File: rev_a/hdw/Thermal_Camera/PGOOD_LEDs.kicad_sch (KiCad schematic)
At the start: 21 parts, among them U1501 74LVC1G97, U1502 74LVC1G97, U1503 74LVC1G97, U1504 74LVC1G97, U1505 74LVC1G97

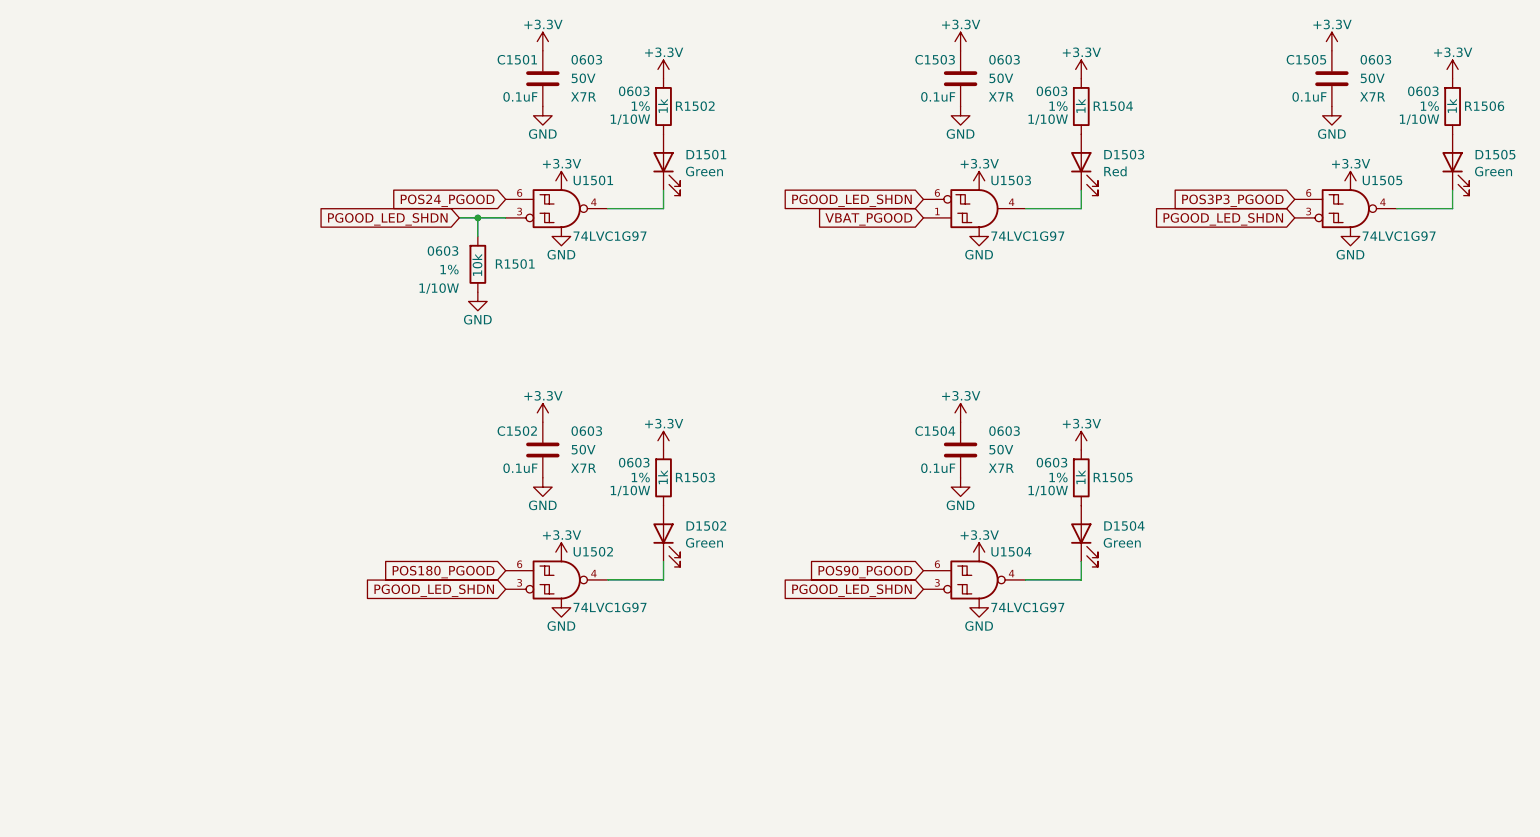
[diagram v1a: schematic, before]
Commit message: added many more blank schematic sheets
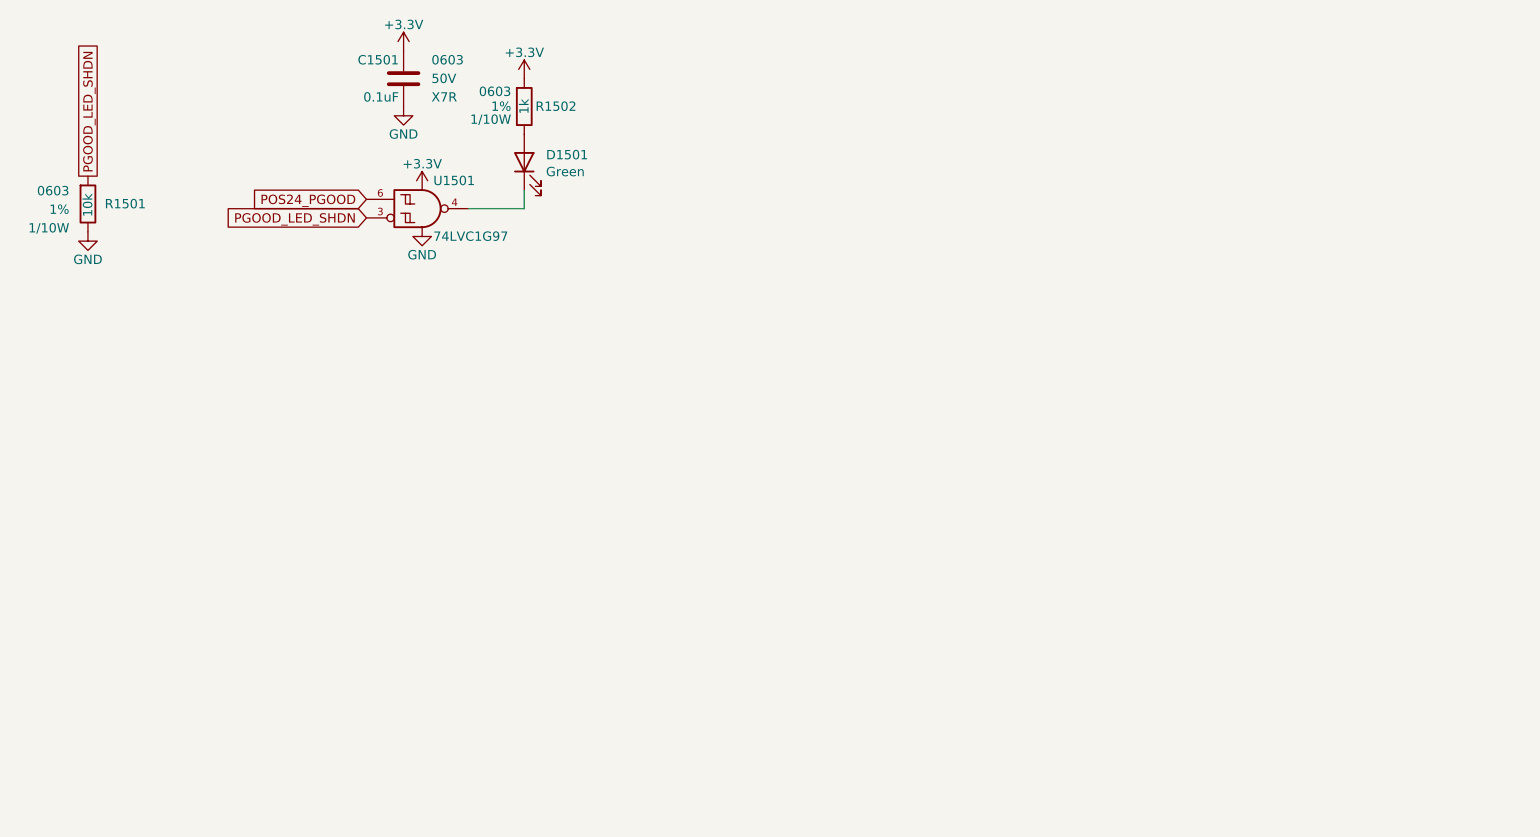
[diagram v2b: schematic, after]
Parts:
- removed C1502, C1503, C1504, C1505: 0.1uF, Capacitors_SMD:C_0603, symbol Custom_Library:C_Custom
- removed D1502, D1504, D1505: Green, LEDs:LED_0603, symbol Device:LED
- removed D1503: Red, LEDs:LED_0603, symbol Device:LED
- removed R1503, R1504, R1505, R1506: 1k, Resistors_SMD:R_0603, symbol Custom_Library:R_Custom
- removed U1502, U1504, U1505: 74LVC1G97, Package_TO_SOT_SMD:SOT-363_SC-70-6, symbol Custom_Library:74LVC1G97_Power_NAND_INV
- removed U1503: 74LVC1G97, Package_TO_SOT_SMD:SOT-363_SC-70-6, symbol Custom_Library:74LVC1G97_Power_AND_INV
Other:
- moved on the sheet: C1501, D1501, R1501, R1502, U1501

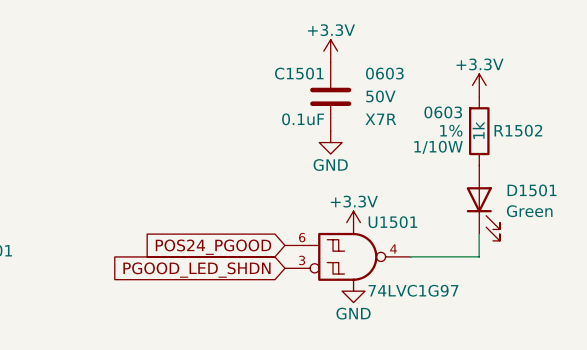
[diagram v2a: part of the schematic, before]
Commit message: changed a lot of circuits from +3.3V to +3.0V VDD
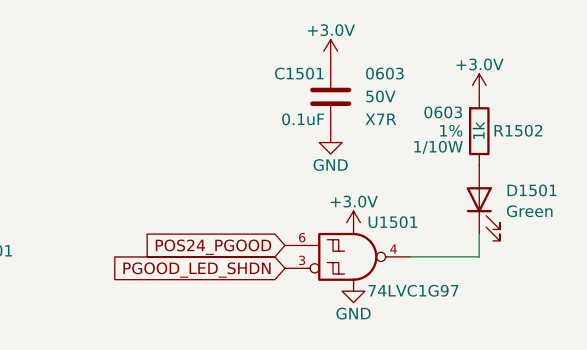
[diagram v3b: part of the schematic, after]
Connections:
- net +3.3V renamed +3.0V
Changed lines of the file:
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@@
     )
   )
-  (symbol (lib_id "power:+3.3V") (at 72.39 54.61 0) (unit 1)
-    (in_bom yes) (on_board yes) (dnp no)
-    (property "Reference" "#PWR01511" (at 72.39 58.42 0)
-      (effects (font (size 1.27 1.27)) hide)
-    )
-    (property "Value" "+3.3V" (at 72.39 51.054 0)
+  (symbol (lib_id "Custom Library:+3.0V") (at 72.39 54.61 0) (unit 1)
+    (in_bom yes) (on_board yes) (dnp no)
+    (property "Reference" "#PWR02603" (at 72.39 58.42 0)
+      (effects (font (size 1.27 1.27)) hide)
+    )
+    (property "Value" "+3.0V" (at 72.39 51.054 0)
       (effects (font (size 1.27 1.27)))
     )
@@
     (pin "1")
     (instances
-      (project "Nixie_Clock_Core"
-        (path "/16fdce21-b570-4d81-a458-e8839d611806/2cd2cc24-63f3-4ff7-b2ec-a0dfd71a27e5"
-          (reference "#PWR01511") (unit 1)
-        )
-      )
-      (project "LED_Panel_Controller"
-        (path "/22e05ee1-b227-4be7-9418-94433f274720/00000000-0000-0000-0000-00005cb7a8c3"
-          (reference "#PWR?") (unit 1)
-        )
-        (path "/22e05ee1-b227-4be7-9418-94433f274720/00000000-0000-0000-0000-00005f582e4a"
-          (reference "#PWR?") (unit 1)
-        )
-        (path "/22e05ee1-b227-4be7-9418-94433f274720/00000000-0000-0000-0000-00005e93cc4e"
-          (reference "#PWR?") (unit 1)
-        )
-        (path "/22e05ee1-b227-4be7-9418-94433f274720/00000000-0000-0000-0000-00005cb7a8bc"
-          (reference "#PWR?") (unit 1)
-        )
-      )
-      (project "Thermal_Camera"
-        (path "/4bd21e0b-5408-4b93-866e-c82ac5b31fa9/c698b831-0a89-446b-a0f6-e678b516ea4f"
-          (reference "#PWR02006") (unit 1)
+      (project "Thermal_Camera"
+        (path "/4bd21e0b-5408-4b93-866e-c82ac5b31fa9/c698b831-0a89-446b-a0f6-e678b516ea4f"
+          (reference "#PWR02603") (unit 1)
+        )
+      )
+    )
+  )
+  (symbol (lib_id "Custom Library:+3.0V") (at 86.36 39.37 0) (unit 1)
+    (in_bom yes) (on_board yes) (dnp no)
+    (property "Reference" "#PWR02602" (at 86.36 43.18 0)
+      (effects (font (size 1.27 1.27)) hide)
+    )
+    (property "Value" "+3.0V" (at 86.36 35.814 0)
+      (effects (font (size 1.27 1.27)))
+    )
+    (property "Footprint" "" (at 86.36 39.37 0)
+      (effects (font (size 1.27 1.27)) hide)
+    )
+    (property "Datasheet" "" (at 86.36 39.37 0)
+      (effects (font (size 1.27 1.27)) hide)
+    )
+    (pin "1")
+    (instances
+      (project "Thermal_Camera"
+        (path "/4bd21e0b-5408-4b93-866e-c82ac5b31fa9/c698b831-0a89-446b-a0f6-e678b516ea4f"
+          (reference "#PWR02602") (unit 1)
         )
       )
@@
     )
   )
-  (symbol (lib_id "power:+3.3V") (at 86.36 39.37 0) (unit 1)
-    (in_bom yes) (on_board yes) (dnp no)
-    (property "Reference" "#PWR01515" (at 86.36 43.18 0)
-      (effects (font (size 1.27 1.27)) hide)
-    )
-    (property "Value" "+3.3V" (at 86.36 35.814 0)
-      (effects (font (size 1.27 1.27)))
-    )
-    (property "Footprint" "" (at 86.36 39.37 0)
-      (effects (font (size 1.27 1.27)) hide)
-    )
-    (property "Datasheet" "" (at 86.36 39.37 0)
-      (effects (font (size 1.27 1.27)) hide)
-    )
-    (pin "1")
-    (instances
-      (project "Nixie_Clock_Core"
-        (path "/16fdce21-b570-4d81-a458-e8839d611806/2cd2cc24-63f3-4ff7-b2ec-a0dfd71a27e5"
-          (reference "#PWR01515") (unit 1)
-        )
-      )
-      (project "LED_Panel_Controller"
-        (path "/22e05ee1-b227-4be7-9418-94433f274720/00000000-0000-0000-0000-00005cb7a8c3"
-          (reference "#PWR?") (unit 1)
-        )
-        (path "/22e05ee1-b227-4be7-9418-94433f274720/00000000-0000-0000-0000-00005f582e4a"
-          (reference "#PWR?") (unit 1)
-        )
-        (path "/22e05ee1-b227-4be7-9418-94433f274720/00000000-0000-0000-0000-00005e93cc4e"
-          (reference "#PWR?") (unit 1)
-        )
-        (path "/22e05ee1-b227-4be7-9418-94433f274720/00000000-0000-0000-0000-00005cb7a8bc"
-          (reference "#PWR?") (unit 1)
-        )
-      )
-      (project "Thermal_Camera"
-        (path "/4bd21e0b-5408-4b93-866e-c82ac5b31fa9/c698b831-0a89-446b-a0f6-e678b516ea4f"
-          (reference "#PWR02010") (unit 1)
-        )
-      )
-    )
-  )
-  (symbol (lib_id "power:+3.3V") (at 69.85 35.56 0) (unit 1)
-    (in_bom yes) (on_board yes) (dnp no)
-    (property "Reference" "#PWR01507" (at 69.85 39.37 0)
-      (effects (font (size 1.27 1.27)) hide)
-    )
-    (property "Value" "+3.3V" (at 69.85 32.004 0)
-      (effects (font (size 1.27 1.27)))
-    )
-    (property "Footprint" "" (at 69.85 35.56 0)
-      (effects (font (size 1.27 1.27)) hide)
-    )
-    (property "Datasheet" "" (at 69.85 35.56 0)
-      (effects (font (size 1.27 1.27)) hide)
-    )
-    (pin "1")
-    (instances
-      (project "Nixie_Clock_Core"
-        (path "/16fdce21-b570-4d81-a458-e8839d611806/2cd2cc24-63f3-4ff7-b2ec-a0dfd71a27e5"
-          (reference "#PWR01507") (unit 1)
-        )
-      )
-      (project "LED_Panel_Controller"
-        (path "/22e05ee1-b227-4be7-9418-94433f274720/00000000-0000-0000-0000-00005cb7a8c3"
-          (reference "#PWR?") (unit 1)
-        )
-        (path "/22e05ee1-b227-4be7-9418-94433f274720/00000000-0000-0000-0000-00005f582e4a"
-          (reference "#PWR?") (unit 1)
-        )
-        (path "/22e05ee1-b227-4be7-9418-94433f274720/00000000-0000-0000-0000-00005e93cc4e"
-          (reference "#PWR?") (unit 1)
-        )
-        (path "/22e05ee1-b227-4be7-9418-94433f274720/00000000-0000-0000-0000-00005cb7a8bc"
-          (reference "#PWR?") (unit 1)
-        )
-      )
-      (project "Thermal_Camera"
-        (path "/4bd21e0b-5408-4b93-866e-c82ac5b31fa9/c698b831-0a89-446b-a0f6-e678b516ea4f"
-          (reference "#PWR02002") (unit 1)
-        )
-      )
-    )
-  )
   (symbol (lib_id "Custom_Library:C_Custom") (at 69.85 39.37 0) (mirror y) (unit 1)
     (in_bom yes) (on_board yes) (dnp no)
@@
         )
       )
+    )
+  )
+  (symbol (lib_id "Custom Library:+3.0V") (at 69.85 35.56 0) (unit 1)
+    (in_bom yes) (on_board yes) (dnp no)
+    (property "Reference" "#PWR02601" (at 69.85 39.37 0)
+      (effects (font (size 1.27 1.27)) hide)
+    )
+    (property "Value" "+3.0V" (at 69.85 32.004 0)
+      (effects (font (size 1.27 1.27)))
+    )
+    (property "Footprint" "" (at 69.85 35.56 0)
+      (effects (font (size 1.27 1.27)) hide)
+    )
+    (property "Datasheet" "" (at 69.85 35.56 0)
+      (effects (font (size 1.27 1.27)) hide)
+    )
+    (pin "1")
+    (instances
+      (project "Thermal_Camera"
+        (path "/4bd21e0b-5408-4b93-866e-c82ac5b31fa9/c698b831-0a89-446b-a0f6-e678b516ea4f"
+          (reference "#PWR02601") (unit 1)
+        )
+      )

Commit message: added some more USB stuff
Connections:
- net POS24_PGOOD renamed POS12_PGOOD
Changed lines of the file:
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@@
     )
   )
-  (global_label "POS24_PGOOD" (shape input) (at 64.77 55.88 180) (fields_autoplaced)
+  (global_label "POS12_PGOOD" (shape input) (at 64.77 55.88 180) (fields_autoplaced)
     (effects (font (size 1.27 1.27)) (justify right))
     (property "Intersheetrefs" "${INTERSHEET_REFS}" (at 48.1966 55.88 0)

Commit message: lots of random schematic progress
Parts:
- added C1501 (x5): 0.1uF, Capacitors_SMD:C_0603, symbol Custom_Library:C_Custom
- added D1501 (x5): Green, LEDs:LED_0603, symbol Device:LED
- added R1502 (x5): 1k, Resistors_SMD:R_0603, symbol Custom_Library:R_Custom
- added U1501 (x4): 74LVC1G97, Package_TO_SOT_SMD:SOT-363_SC-70-6, symbol Custom_Library:74LVC1G97_Power_NAND_INV
- added U?: 74LVC1G97, Package_TO_SOT_SMD:SOT-363_SC-70-6, symbol Custom Library:74LVC1G97_Power_NOT
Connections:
- net +3.0V: now also C1501.1, C1501.1, C1501.1, C1501.1, R1502.1, R1502.1, R1502.1, R1502.1, U1501.1 (VCC), U1501.1 (VCC), U1501.1 (VCC), U1501.1 (VCC), U1501.5 (VCC), U1501.5 (VCC), U1501.5 (VCC), U1501.5 (VCC)
- net GND: now also C1501.2, C1501.2, C1501.2, C1501.2, C1501.2, U1501.2 (GND), U1501.2 (GND), U1501.2 (GND), U1501.2 (GND), U?.2 (GND), U?.3 (GND)
- net PGOOD_LED_SHDN: now also U1501.3, U1501.3, U1501.3, U1501.3
- new net: D1501.2 (A), R1502.2 (x5)
- new net: D1501.1 (K), U1501.4 (x4)
- new net: D1501.1 (K), U?.4
- new net +3.3V_USB: C1501.1, R1502.1, U?.1 (VCC), U?.5 (VCC)
- new net POS1P2_PGOOD: U1501.6
- new net POS1P8_PGOOD: U1501.6
- new net POS2P8_PGOOD: U1501.6
- new net POS3P0_PGOOD: U1501.6
- new net POS3P3_USB_PGOOD: U?.6

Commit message: worked on some battery stuff
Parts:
- added C?: 0.1uF, Capacitors_SMD:C_0603, symbol Custom_Library:C_Custom
- added D?: Red, LEDs:LED_0603, symbol Device:LED
- added R?: 1k, Resistors_SMD:R_0603, symbol Custom_Library:R_Custom
- added U?: 74LVC1G97, Package_TO_SOT_SMD:SOT-363_SC-70-6, symbol Custom_Library:74LVC1G97_Power_NAND_INV
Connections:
- net +3.0V: now also C?.1, R?.1, U?.1 (VCC), U?.5 (VCC)
- net BATT_LOWBAT: now also U?.6
- net GND: now also C?.2, U?.2 (GND)
- net PGOOD_LED_SHDN: now also U?.3
- new net: D?.2 (A), R?.2
- new net: D?.1 (K), U?.4
